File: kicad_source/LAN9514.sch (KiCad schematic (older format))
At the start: 46 parts, among them J1 RJ45-TRANSFO-2, P1 USB_2.0_Connector, SW1 SW_PUSH, U2 LAN9514, U3 MIC2026, U5 93LC66, Y1 25MHz

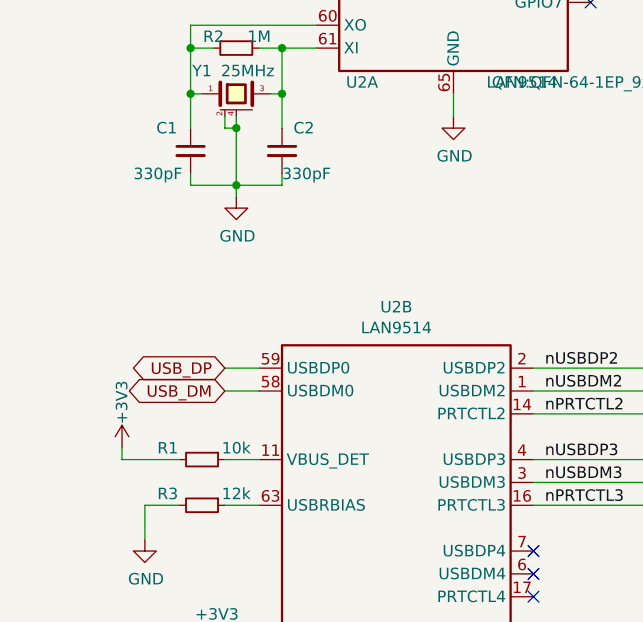
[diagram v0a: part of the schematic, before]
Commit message: tested and fixed last bugs
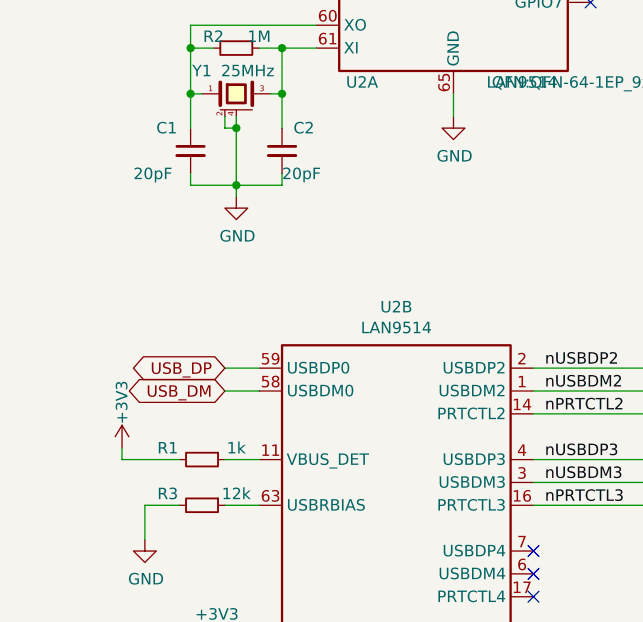
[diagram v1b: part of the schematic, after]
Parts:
- C1, C2: value 330pF -> 20pF
- R1: value 10k -> 1k
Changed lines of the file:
@@
 P 1100 4250
 F 0 "C1" H 950 4350 50  0000 L CNN
-F 1 "330pF" H 850 4150 50  0000 L CNN
+F 1 "20pF" H 850 4150 50  0000 L CNN
 F 2 "capacitors:C_0603" H 1100 4100 50  0001 C CNN
 F 3 "" H 1100 4250 50  0000 C CNN
@@
 P 1500 4250
 F 0 "C2" H 1550 4350 50  0000 L CNN
-F 1 "330pF" H 1500 4150 50  0000 L CNN
+F 1 "20pF" H 1500 4150 50  0000 L CNN
 F 2 "capacitors:C_0603" H 1500 4100 50  0001 C CNN
 F 3 "" H 1500 4250 50  0000 C CNN
@@
 P 1150 5600
 F 0 "R1" V 1100 5450 50  0000 C CNN
-F 1 "10k" V 1100 5750 50  0000 C CNN
+F 1 "1k" V 1100 5750 50  0000 C CNN
 F 2 "resistors:R_0603" H 1150 5450 50  0001 C CNN
 F 3 "" H 1150 5600 50  0000 C CNN
